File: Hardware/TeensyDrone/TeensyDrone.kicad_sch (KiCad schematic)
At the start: 20 parts, among them J1 Conn_01x04, J2 Conn_01x08, J3 Conn_01x04, U1 DEV-15583

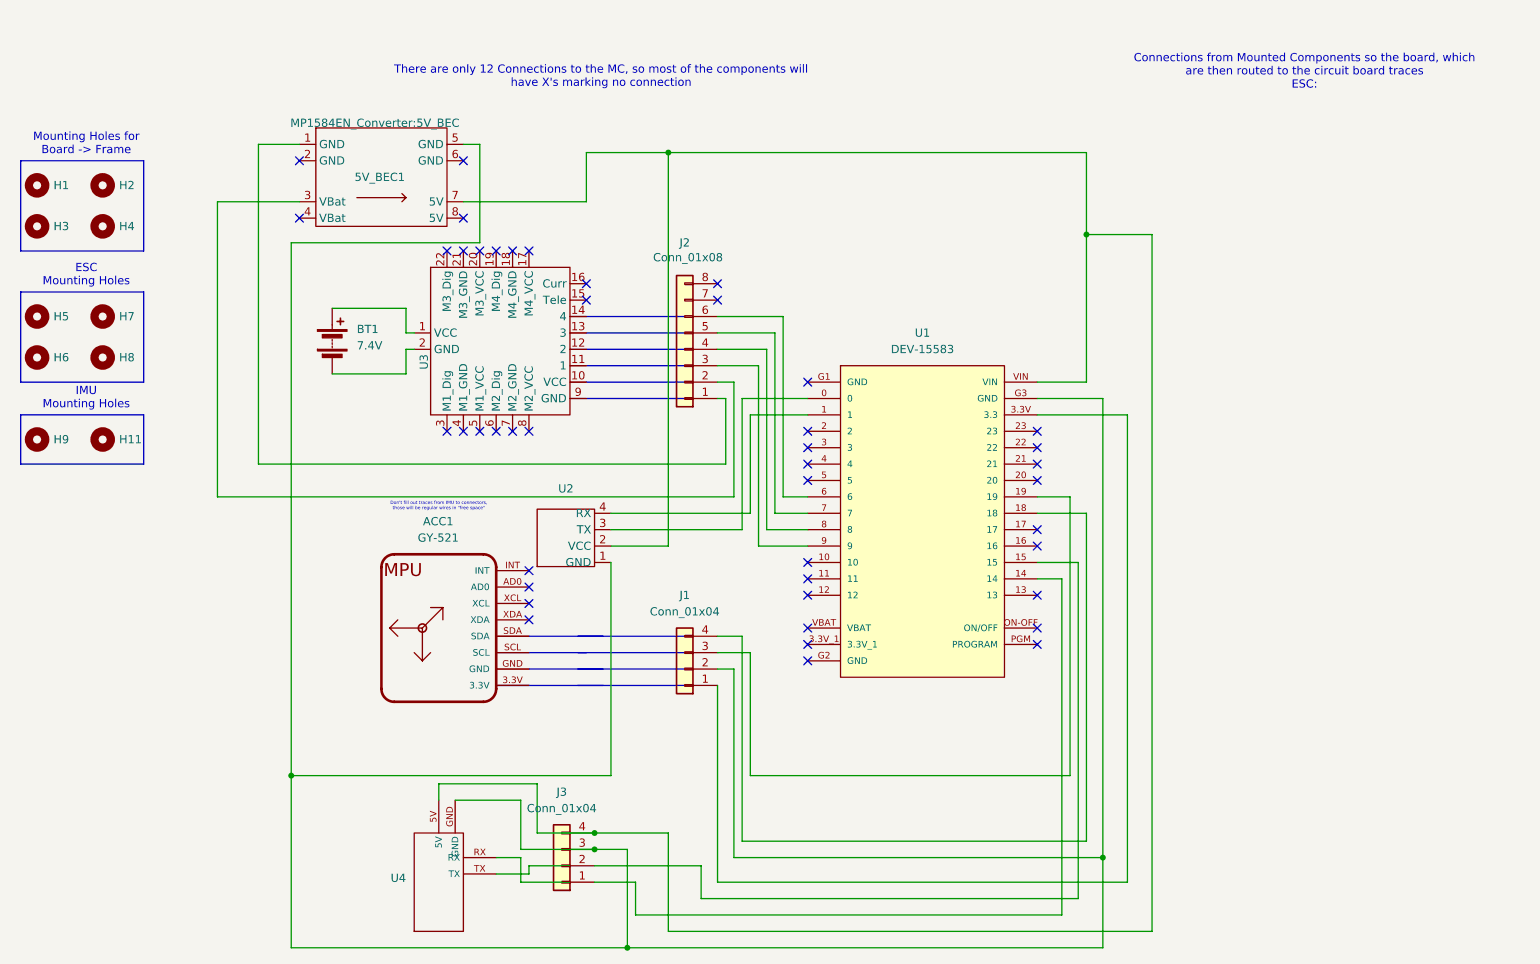
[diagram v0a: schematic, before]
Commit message: Revert "Moved to Teensy 4.0 from 4.1"
This reverts commit 64f42becbd12878e856e1dc259d1d069ff850610.
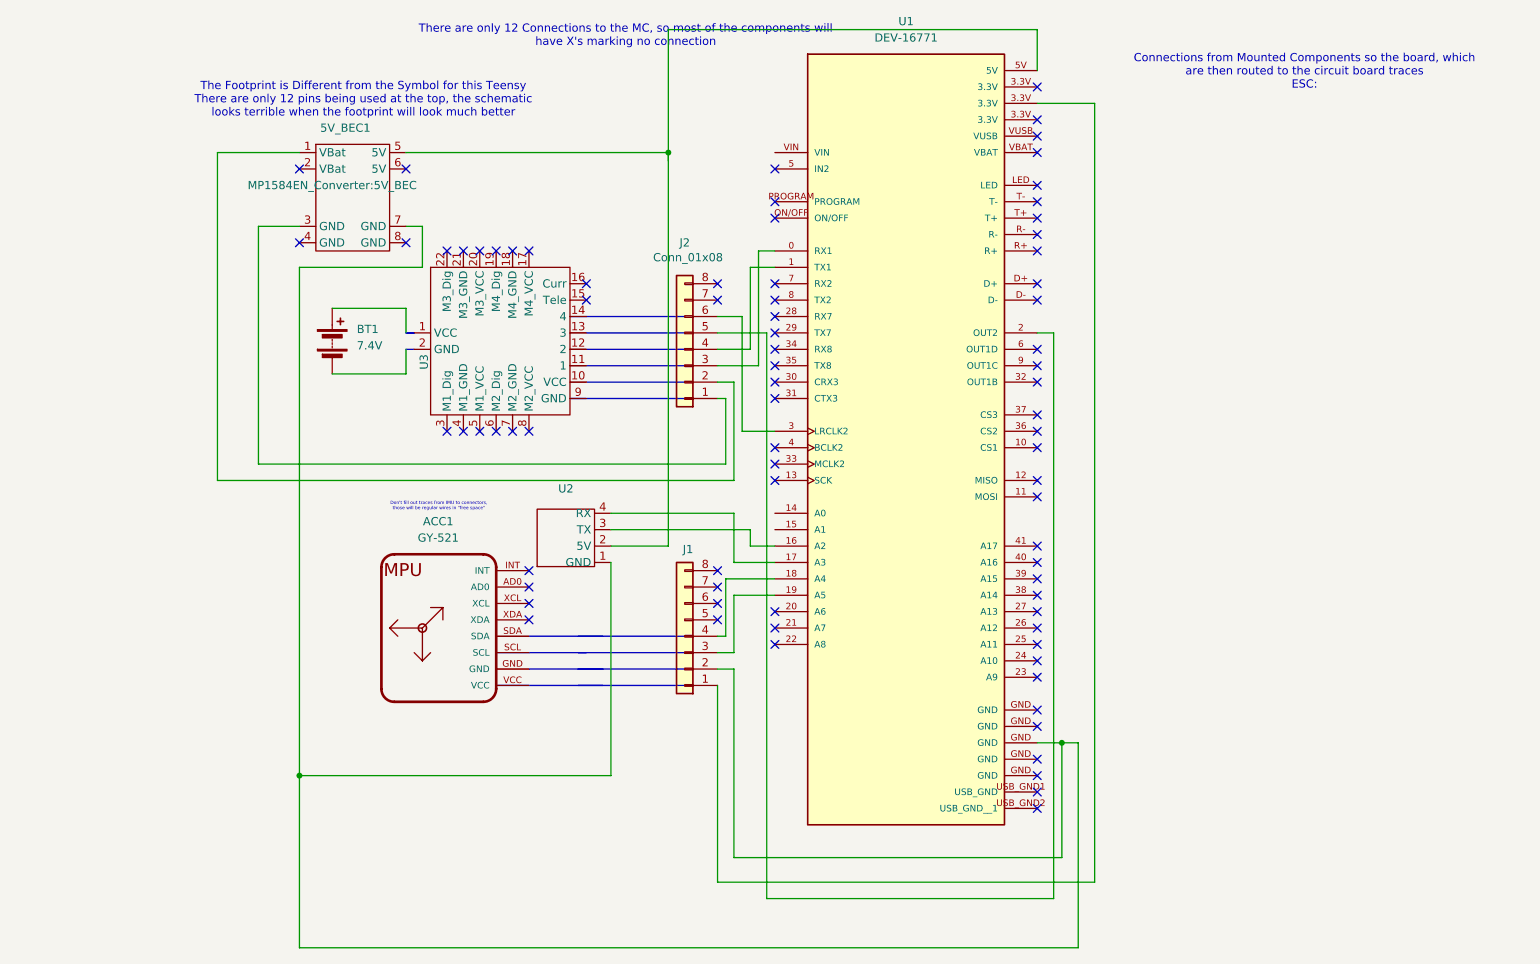
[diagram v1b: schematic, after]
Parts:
- removed H1, H2, H3, H4, H5, H6, H7, H8: MountingHole, MountingHole:MountingHole_2mm, symbol Mechanical:MountingHole
- removed H11, H9: MountingHole, MountingHole:MountingHole_3.2mm_M3, symbol Mechanical:MountingHole
- removed J1, J3: Conn_01x04, Connector_PinHeader_2.54mm:PinHeader_1x04_P2.54mm_Vertical, symbol Connector_Generic:Conn_01x04
- removed U1: DEV-15583, DEV-15583:MODULE_DEV-15583, symbol Teensy 4.0:DEV-15583
- removed U4: ~, symbol MatekOpticalFlow:3901-L0X
- added J1: Conn_01x08, Connector_PinHeader_2.54mm:PinHeader_1x08_P2.54mm_Vertical, symbol Connector_Generic:Conn_01x08
- added U1: DEV-16771, Teensy 4.1:MODULE_DEV-16771, symbol DEV-16771:DEV-16771
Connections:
- net at 5V_BEC1.5 (5V): now also U2.2 (5V), U1.5V; no longer U2.1 (GND)
- net at 5V_BEC1.7 (GND): now also U2.1 (GND), J1.2 (GND), U1.GND; no longer U2.2 (VCC)
- net at U2.3 (TX): now also U1.16 (A2)
- net at U2.4 (RX): now also U1.17 (A3)
- net at J2.6 (Servo4): now also U1.3 (LRCLK2)
- net at J2.5 (Servo3): now also U1.2 (OUT2)
- net at J2.4 (Servo2): now also U1.1 (TX1)
- net at J2.3 (Servo1): now also U1.0 (RX1)
- net at BT1.1 (+): no longer U3.1 (VCC)
- net at BT1.2 (-): no longer U3.2 (GND)
- net at 5V_BEC1.1 (VBat): now also J2.2 (VBat); no longer J2.1 (Pin_1)
- net at 5V_BEC1.3 (GND): now also J2.1 (GND); no longer J2.2 (Pin_2)
- new net: J1.4 (SDA), U1.18 (A4)
- new net: J1.3 (SCL), U1.19 (A5)
- new net: J1.1 (3.3V), U1.3.3V
- no-connect marks 44 -> 79
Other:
- note added: "The Footprint is Different from the Symbol for this Teensy There are only 12 pins being used at the top, the schematic looks terrible when the footprint will look much better"
- note removed: "ESC Mounting Holes"
- note removed: "IMU Mounting Holes"
- note removed: "Mounting Holes for Board -> Frame"
- company: University of Maryland : MATRIX Lab -> (none)
- title: Teensy Drone -> (none)

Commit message: Moved to Teensy 4.0 from 4.1
Signed-off-by: lucas <mtglucas1@gmail.com>
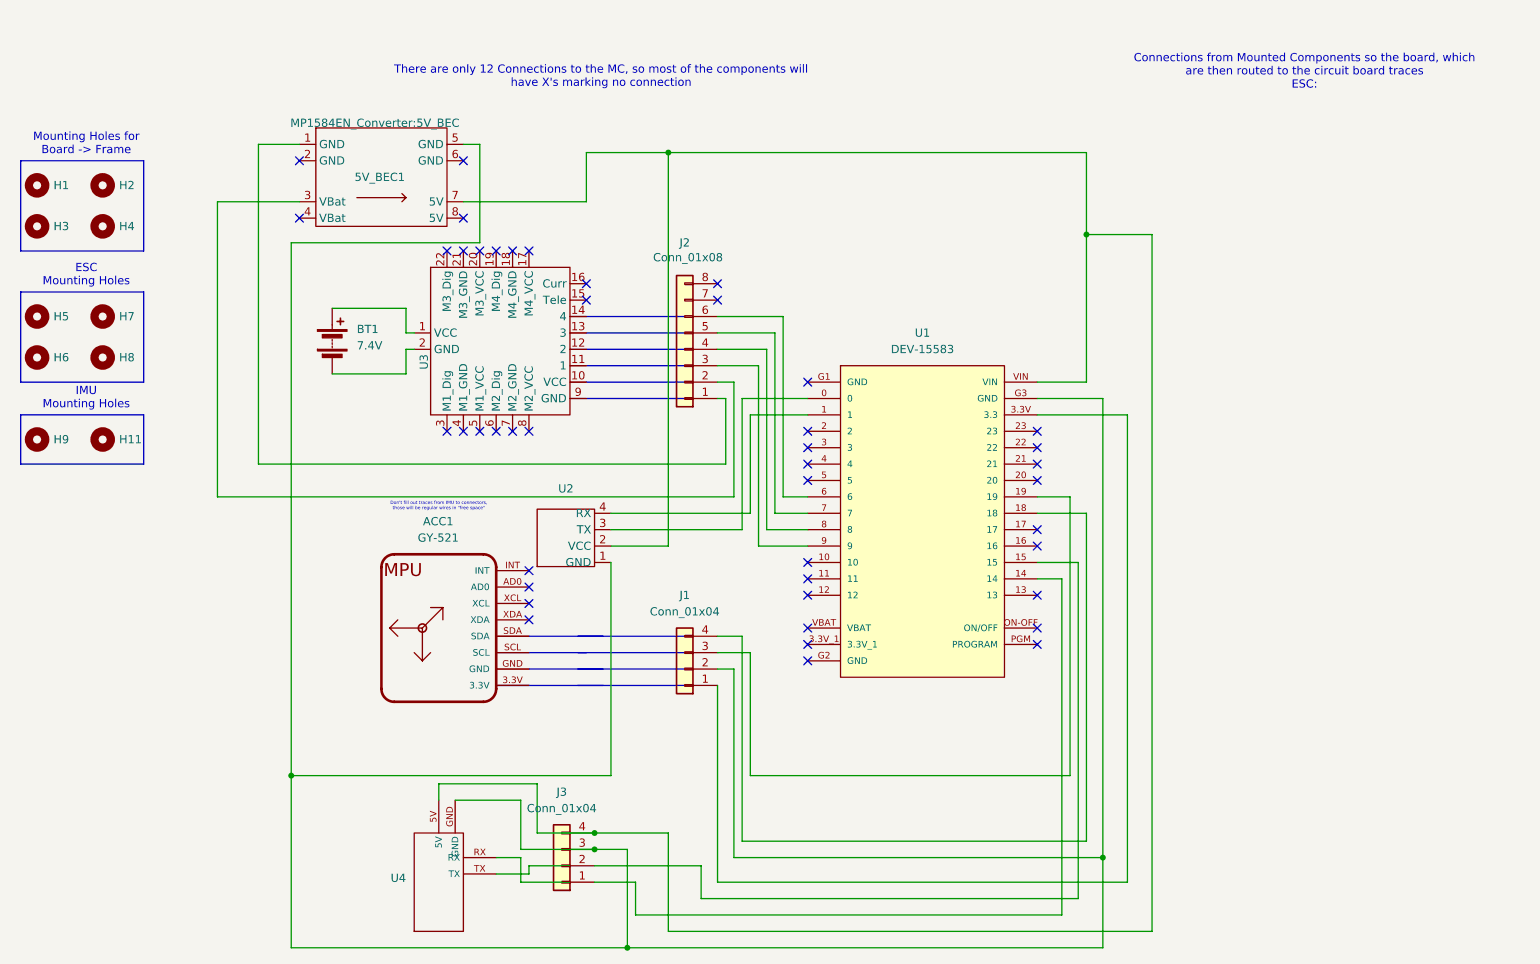
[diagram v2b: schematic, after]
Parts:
- removed J1: Conn_01x08, Connector_PinHeader_2.54mm:PinHeader_1x08_P2.54mm_Vertical, symbol Connector_Generic:Conn_01x08
- removed U1: DEV-16771, Teensy 4.1:MODULE_DEV-16771, symbol DEV-16771:DEV-16771
- added H1, H2, H3, H4, H5, H6, H7, H8: MountingHole, MountingHole:MountingHole_2mm, symbol Mechanical:MountingHole
- added H11, H9: MountingHole, MountingHole:MountingHole_3.2mm_M3, symbol Mechanical:MountingHole
- added J1, J3: Conn_01x04, Connector_PinHeader_2.54mm:PinHeader_1x04_P2.54mm_Vertical, symbol Connector_Generic:Conn_01x04
- added U1: DEV-15583, DEV-15583:MODULE_DEV-15583, symbol Teensy 4.0:DEV-15583
- added U4: ~, symbol MatekOpticalFlow:3901-L0X
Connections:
- net at J2.3 (Pin_3): now also U1.9
- net at J2.4 (Pin_4): now also U1.8
- net at U2.3 (TX): now also U1.0
- net at U2.4 (RX): now also U1.1
- net at J2.5 (Pin_5): now also U1.7
- net at J2.6 (Pin_6): now also U1.6
- net at 5V_BEC1.5 (GND): now also U2.1 (GND), J1.2 (Pin_2), J3.3 (GND), U1.G3 (GND), U4.GND; no longer U2.2 (5V)
- net at 5V_BEC1.7 (5V): now also U2.2 (VCC), J3.4 (5V), U1.VIN, U4.5V; no longer U2.1 (GND)
- net at BT1.1 (+): now also U3.1 (VCC)
- net at BT1.2 (-): now also U3.2 (GND)
- net at 5V_BEC1.1 (GND): now also J2.1 (Pin_1); no longer J2.2 (VBat)
- net at 5V_BEC1.3 (VBat): now also J2.2 (Pin_2); no longer J2.1 (GND)
- new net: J3.1 (RX), U1.14
- new net: J3.2 (TX), U1.15
- new net: J1.4 (Pin_4), U1.18
- new net: J1.3 (Pin_3), U1.19
- new net: J1.1 (Pin_1), U1.3.3V (3.3)
- no-connect marks 79 -> 44
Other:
- note added: "ESC Mounting Holes"
- note added: "IMU Mounting Holes"
- note added: "Mounting Holes for Board -> Frame"
- note removed: "The Footprint is Different from the Symbol for this Teensy There are only 12 pins being used at the top, the schematic looks terrible when the footprint will look much better"
- company: (none) -> University of Maryland : MATRIX Lab
- title: (none) -> Teensy Drone
